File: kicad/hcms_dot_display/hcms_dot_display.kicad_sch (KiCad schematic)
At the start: 37 parts, among them J1 Conn_01x13, J2 USB_C_Receptacle_USB2.0, J3 Conn_01x13, J4 Conn_01x13, Q1 Q_PMOS_DSG, Q2 Q_PMOS_DSG, Q3 Q_PMOS_DSG, Q4 Q_PMOS_DSG, Q5 Q_PMOS_DSG, SW2 SW_SPST, U1 ATtiny824-SSF, U2 FT231XS

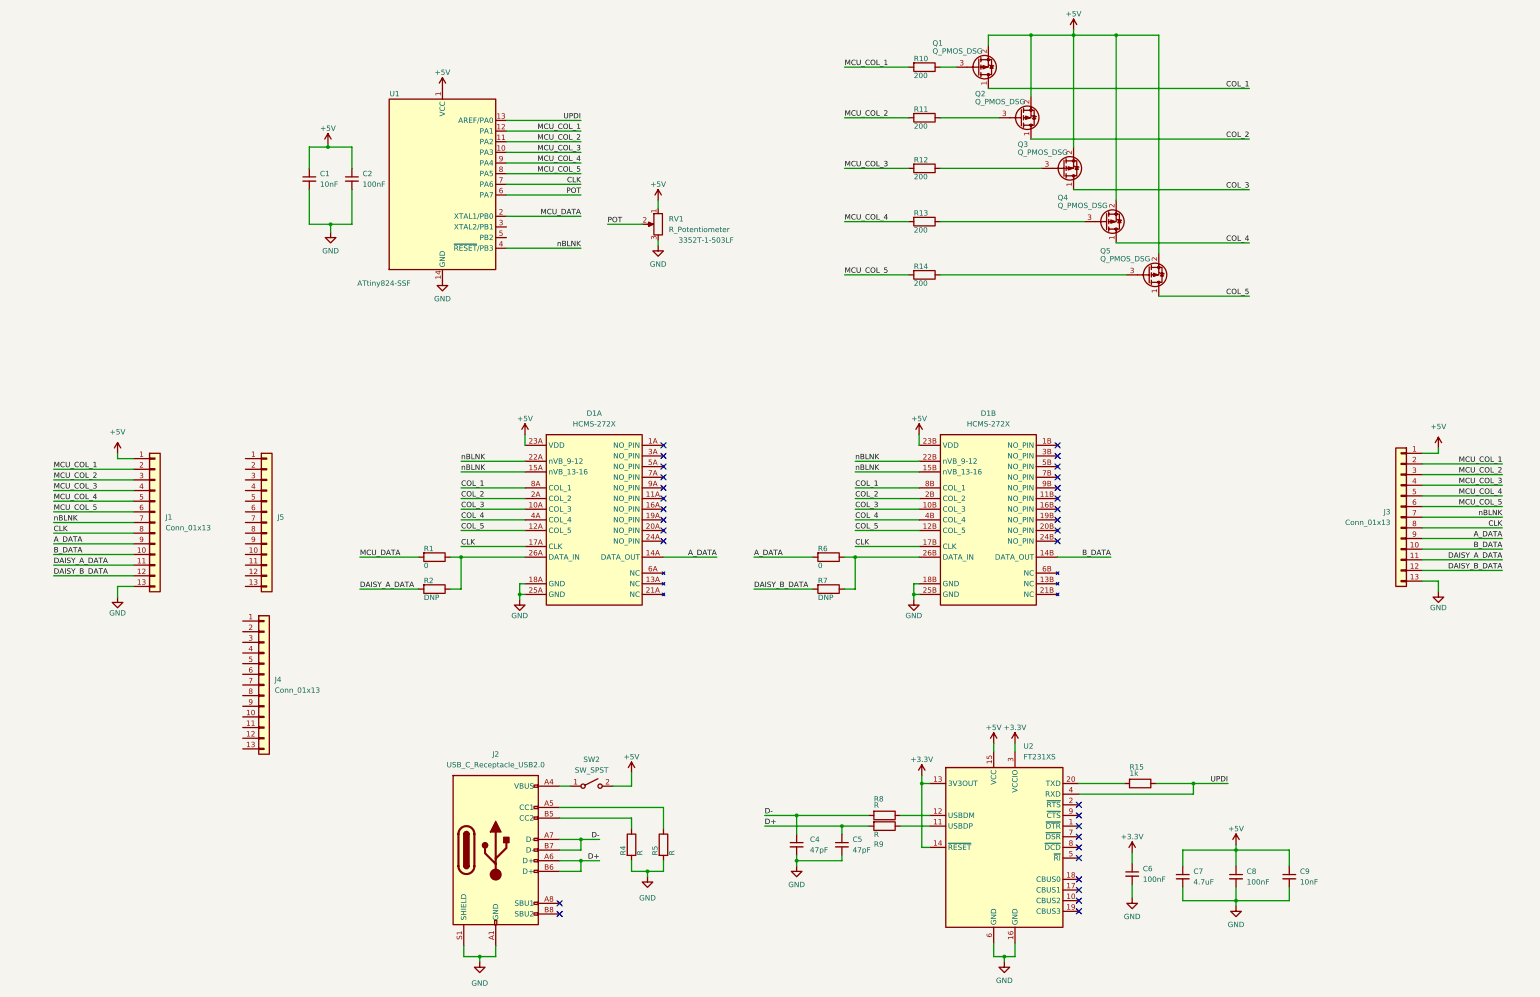
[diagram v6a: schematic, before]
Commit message: Cleaned up layout strat
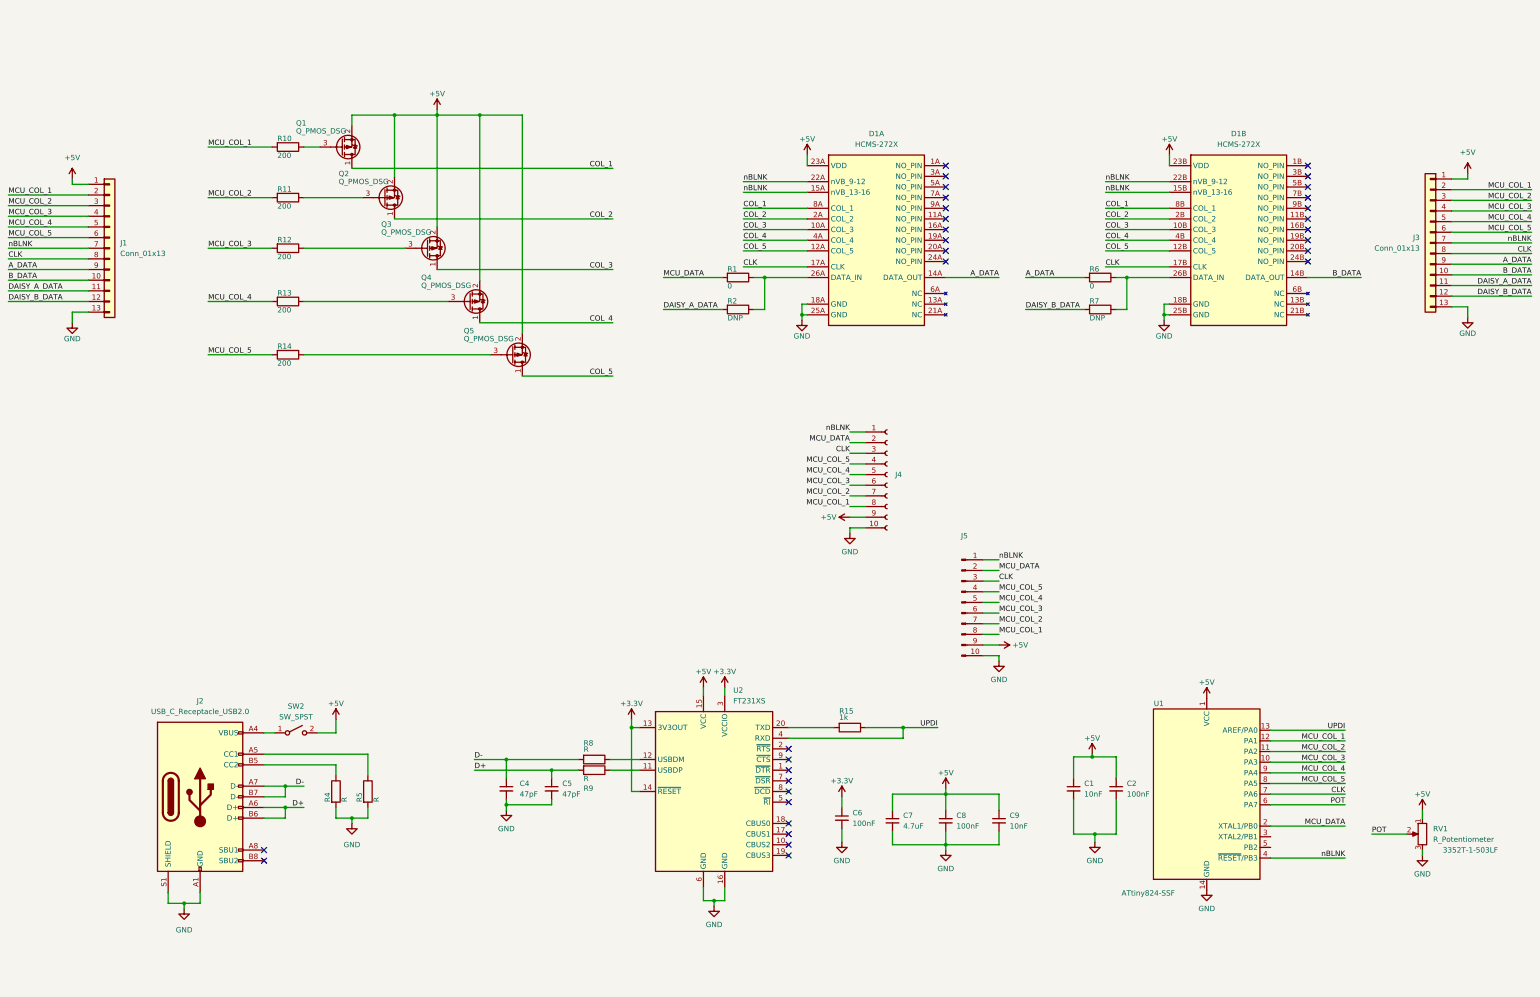
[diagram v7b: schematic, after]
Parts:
- removed J4: Conn_01x13, Connector_PinHeader_2.54mm:PinHeader_1x10_P2.54mm_Vertical, symbol Connector_Generic:Conn_01x13
- removed J5: (no value), symbol Connector_Generic:Conn_01x13
- added J4: (no value), symbol Connector:Conn_01x10_Female
- added J5: (no value), symbol Connector:Conn_01x10_Male
- C1, C2, C4, C5, C6, C7, C8, C9: footprint (none) -> Capacitor_SMD:C_0402_1005Metric
- R1, R10, R11, R12, R13, R14, R15, R2, R4, R5, R6, R7, R8, R9: footprint (none) -> Resistor_SMD:R_0402_1005Metric
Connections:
- net +5V: now also J4.9 (Pin_9), J5.9 (Pin_9)
- net CLK: now also J4.3 (Pin_3), J5.3 (Pin_3)
- net GND: now also J4.10 (Pin_10), J5.10 (Pin_10)
- net MCU_COL_1: now also J4.8 (Pin_8), J5.8 (Pin_8)
- net MCU_COL_2: now also J4.7 (Pin_7), J5.7 (Pin_7)
- net MCU_COL_3: now also J4.6 (Pin_6), J5.6 (Pin_6)
- net MCU_COL_4: now also J4.5 (Pin_5), J5.5 (Pin_5)
- net MCU_COL_5: now also J4.4 (Pin_4), J5.4 (Pin_4)
- net MCU_DATA: now also J4.2 (Pin_2), J5.2 (Pin_2)
- net nBLNK: now also J4.1 (Pin_1), J5.1 (Pin_1)
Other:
- moved on the sheet: C1, C2, C4, C5, C6, C7, C8, C9, D1A, D1B, J1, J2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

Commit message: fixed pot footprint, updated layout from schematics, changed board to board conn sch sym from 13 pin to 11 pin, reorgd sch sym to reflect stacked board design, added decoupling caps to top board
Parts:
- added C10, C11: 10nF, Capacitor_SMD:C_0402_1005Metric, symbol Device:C_Small
- added C3: 100nF, Capacitor_SMD:C_0402_1005Metric, symbol Device:C_Small
- J1, J3: symbol Connector_Generic:Conn_01x13 -> Connector_Generic:Conn_01x11
- J4: value (none) -> Conn_01x10_Female; footprint (none) -> Connector_PinHeader_2.54mm:PinHeader_1x10_P2.54mm_Vertical
- J5: value (none) -> Conn_01x10_Male; footprint (none) -> Connector_PinHeader_2.54mm:PinHeader_1x10_P2.54mm_Vertical
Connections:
- net +5V: now also J4.1 (Pin_1), J5.1 (Pin_1), C10.1, C11.1, C3.1; no longer J4.9 (Pin_9), J5.9 (Pin_9)
- net A_DATA: no longer J1.9 (Pin_9)
- net B_DATA: no longer J1.10 (Pin_10)
- net CLK: now also J4.8 (Pin_8), J5.8 (Pin_8); no longer J4.3 (Pin_3), J5.3 (Pin_3)
- net DAISY_A_DATA: now also J1.9 (Pin_9); no longer J1.11 (Pin_11), J3.11 (Pin_11)
- net DAISY_B_DATA: now also J1.10 (Pin_10); no longer J1.12 (Pin_12), J3.12 (Pin_12)
- net GND: now also J1.11 (Pin_11), J3.11 (Pin_11), C10.2, C11.2, C3.2; no longer J1.13 (Pin_13), J3.13 (Pin_13)
- net MCU_COL_1: now also J4.2 (Pin_2), J5.2 (Pin_2); no longer J4.8 (Pin_8), J5.8 (Pin_8)
- net MCU_COL_2: now also J4.3 (Pin_3), J5.3 (Pin_3); no longer J4.7 (Pin_7), J5.7 (Pin_7)
- net MCU_COL_3: now also J4.4 (Pin_4), J5.4 (Pin_4); no longer J4.6 (Pin_6), J5.6 (Pin_6)
- net MCU_COL_5: now also J4.6 (Pin_6), J5.6 (Pin_6); no longer J4.4 (Pin_4), J5.4 (Pin_4)
- net MCU_DATA: now also J4.9 (Pin_9), J5.9 (Pin_9); no longer J4.2 (Pin_2), J5.2 (Pin_2)
- net nBLNK: now also J4.7 (Pin_7), J5.7 (Pin_7); no longer J4.1 (Pin_1), J5.1 (Pin_1)
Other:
- note added: "BOARD 1 A_DATA -> BOARD 2 DAISY_A_DATA"
- note added: "BOARD 1 B_DATA -> BOARD 2 DAISY_B_DATA"
- note added: "BOTTOM PCB"
- note added: "INCOMING SIGNALS"
- note added: "OUTGOING SIGNALS"
- note added: "TOP PCB"
- moved on the sheet: C1, C2, C4, C5, C6, C7, C8, C9, D1A, D1B, J2, J4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
